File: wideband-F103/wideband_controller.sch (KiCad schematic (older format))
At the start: 107 parts, among them J1 FTSH-107-01-F-DV-K, J2 Conn_02x06_Top_Bottom, J3 Conn_02x02_Odd_Even, J4 Conn_01x10, Q1 VBA2625, Q2 BTS3028, U1 MCP6004, U2 STM32F103C6Tx, U3 OPA388IDR, U4 LM78M05_TO252, U5 XC6206P332MR, U6 REF3033, U7 MCP6002-xSN, U8 TJA1051T-3

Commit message: Addressed issue #19
Added bottom silk for all connector pins.
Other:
- moved on the sheet: C1, C2, C3, C38, C39, C4, C40, C41, C5, C6, J4, R16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

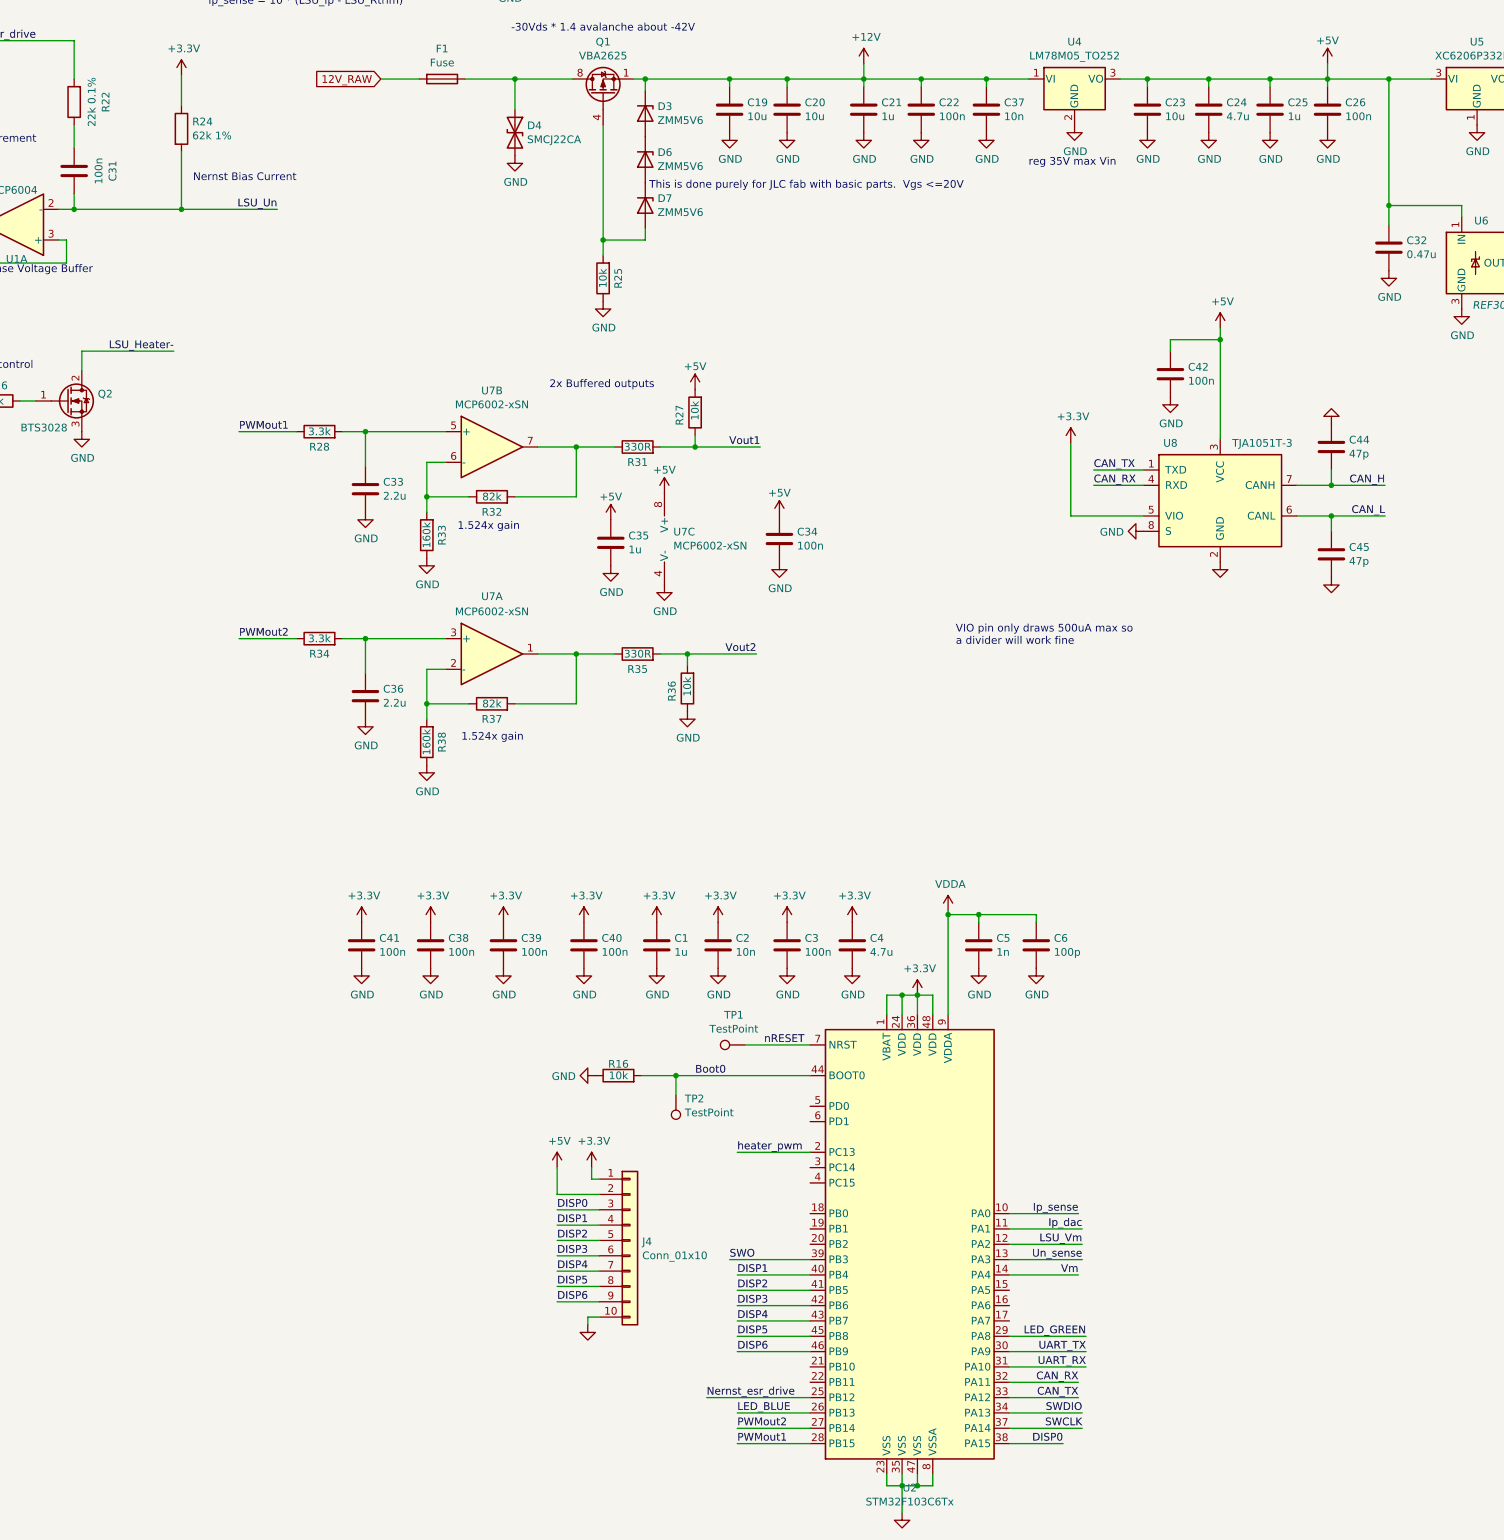
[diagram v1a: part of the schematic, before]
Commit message: 0402 we go!
Changed as many parts as make sense to 0402.  Eliminated several BOM lines.  Added two 0402 solder jumpers for config.  Need to review when less tired.
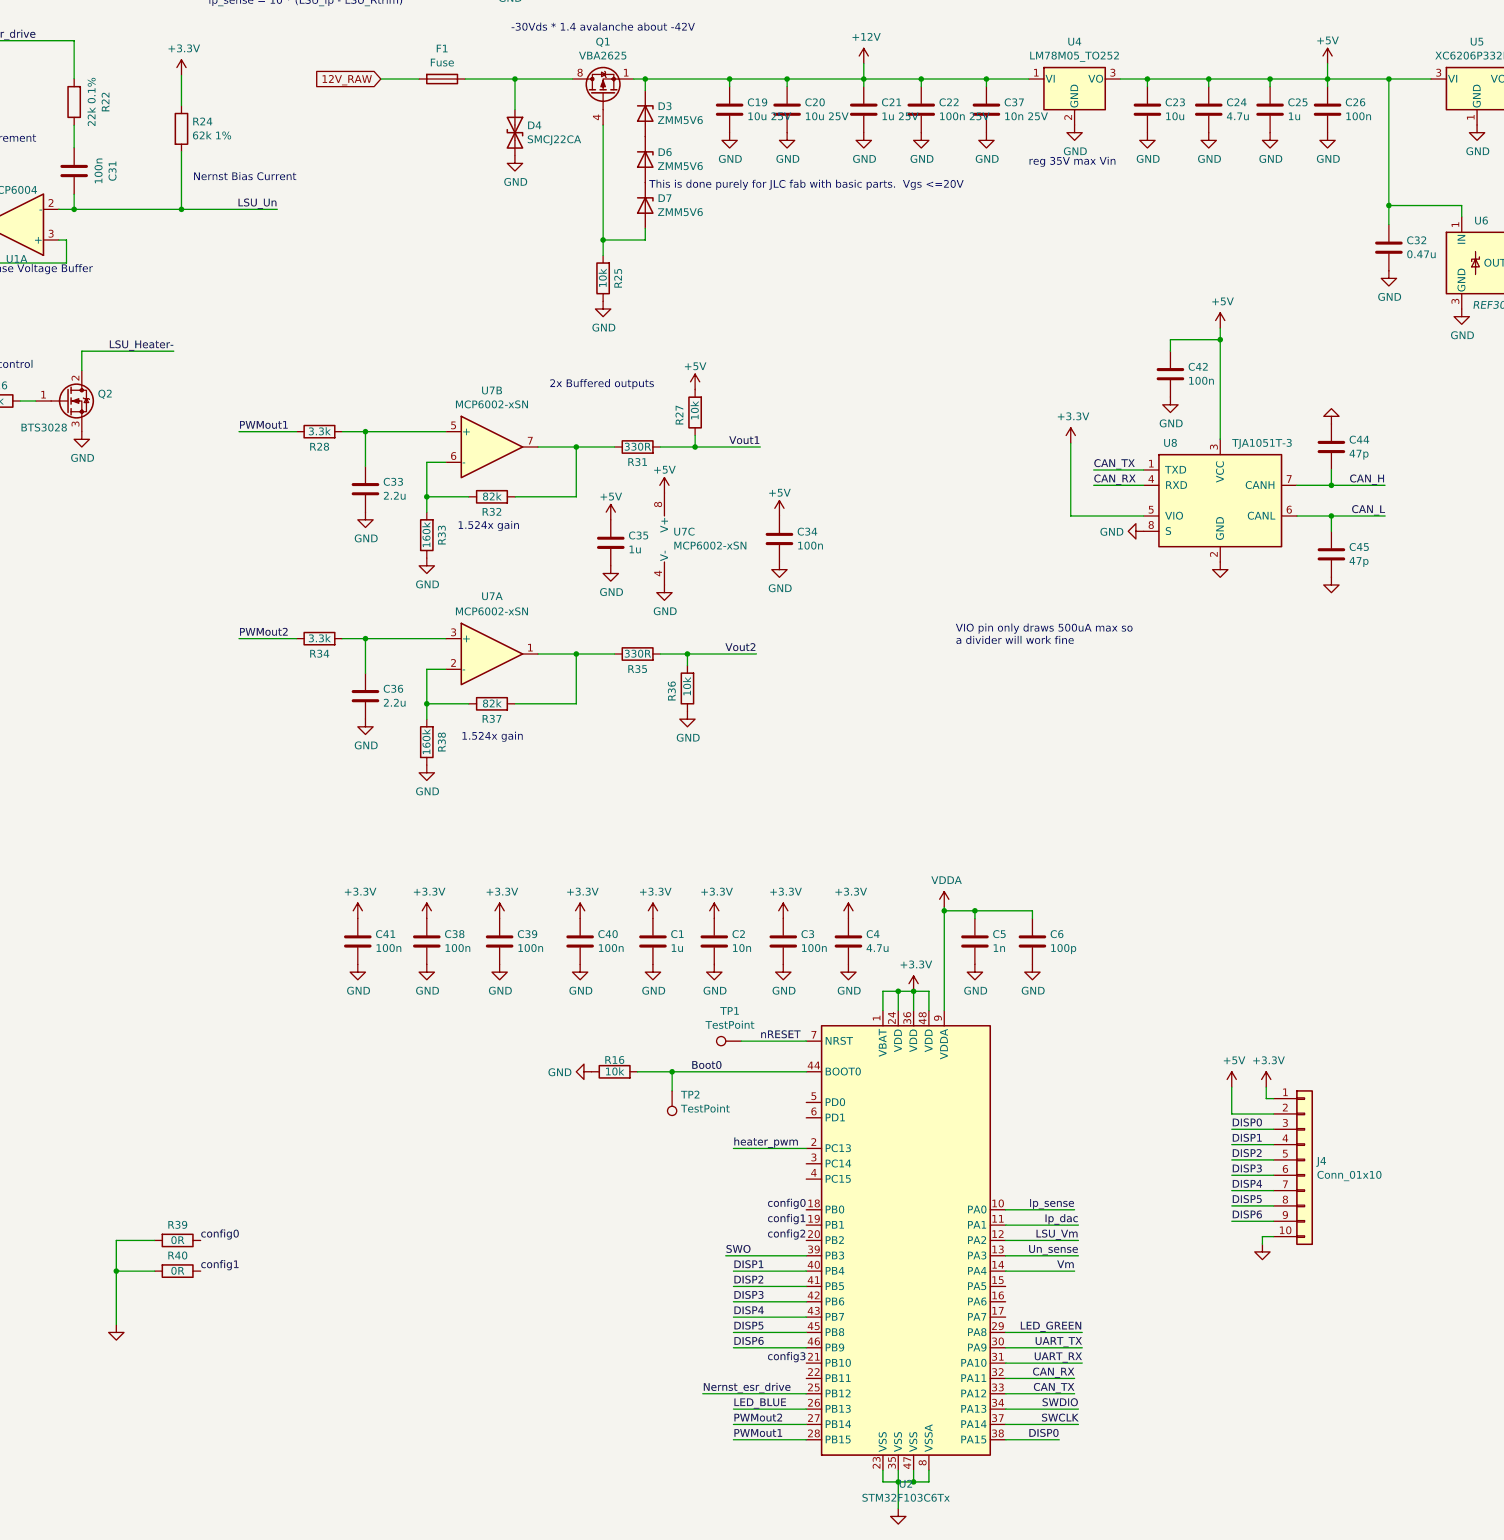
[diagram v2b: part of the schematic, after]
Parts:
- added R39, R40: 0R, Resistor_SMD:R_0402_1005Metric, symbol Device:R
- C1, C10, C25, C28, C35, C7, C8: footprint Capacitor_SMD:C_0603_1608Metric -> Capacitor_SMD:C_0402_1005Metric; LCSC C15849 -> C52923
- C19, C20: value 10u -> 10u 25V
- C21: value 1u -> 1u 25V
- C22: value 100n -> 100n 25V
- C23, C30: footprint Capacitor_SMD:C_0603_1608Metric -> Capacitor_SMD:C_0402_1005Metric; LCSC C19702 -> C15525
- C24, C29, C4: footprint Capacitor_SMD:C_0603_1608Metric -> Capacitor_SMD:C_0402_1005Metric; LCSC C19666 -> C23733
- C32: footprint Capacitor_SMD:C_0603_1608Metric -> Capacitor_SMD:C_0402_1005Metric; LCSC C1623 -> C47339
- C33, C36: footprint Capacitor_SMD:C_0603_1608Metric -> Capacitor_SMD:C_0402_1005Metric; LCSC C23630 -> C12530
- C37: value 10n -> 10n 25V; footprint Capacitor_SMD:C_0603_1608Metric -> Capacitor_SMD:C_0402_1005Metric; LCSC C57112 -> C15195
- R18: footprint Resistor_SMD:R_0603_1608Metric -> Resistor_SMD:R_0402_1005Metric; LCSC C56053 -> 25890
- R28, R34: footprint Resistor_SMD:R_0603_1608Metric -> Resistor_SMD:R_0402_1005Metric; LCSC C22978 -> C25890
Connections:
- net GND: now also R39.2, R40.2
- net config0: now reaches U2.18 (PB0)
- net config0: now also R39.1
- net config1: now reaches U2.19 (PB1)
- net config1: now also R40.1
- net config2: now reaches U2.20 (PB2)
- net config3: now reaches U2.21 (PB10)
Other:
- moved on the sheet: C1, C2, C3, C38, C39, C4, C40, C41, C5, C6, J4, R16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

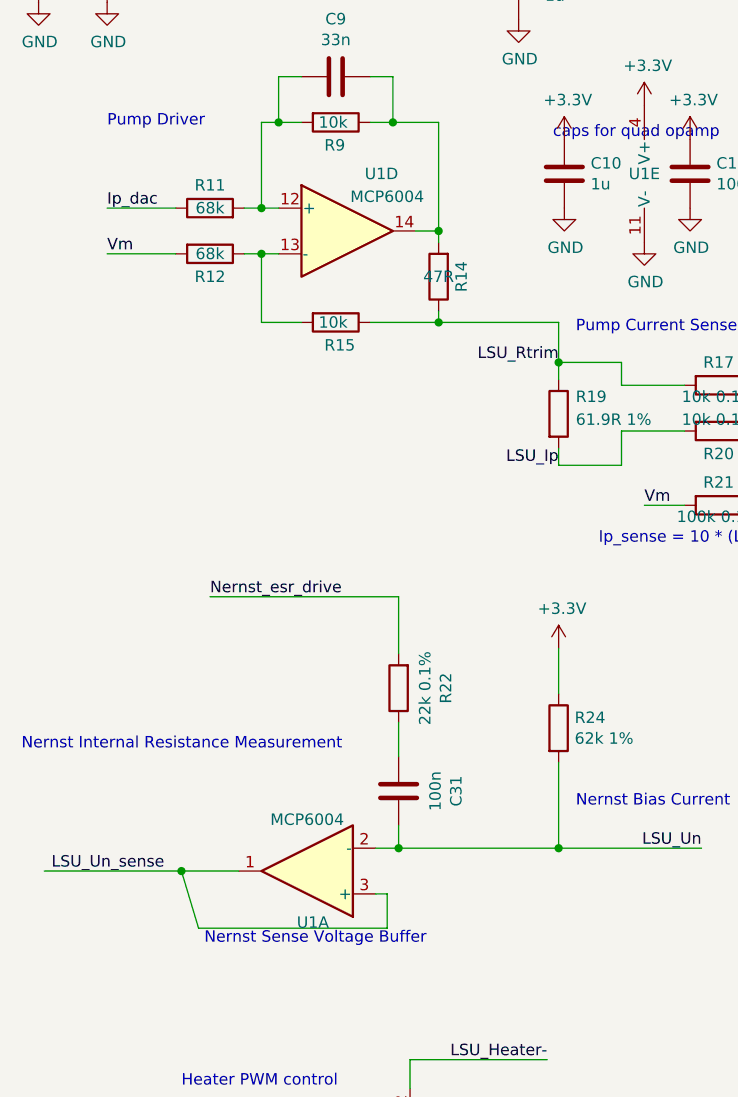
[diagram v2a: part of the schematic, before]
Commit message: Add files via upload
U1A/U1D + and - reversal fixed.  Kept same unobtanium precision op-amp for now.  Incorporates config jumper additions
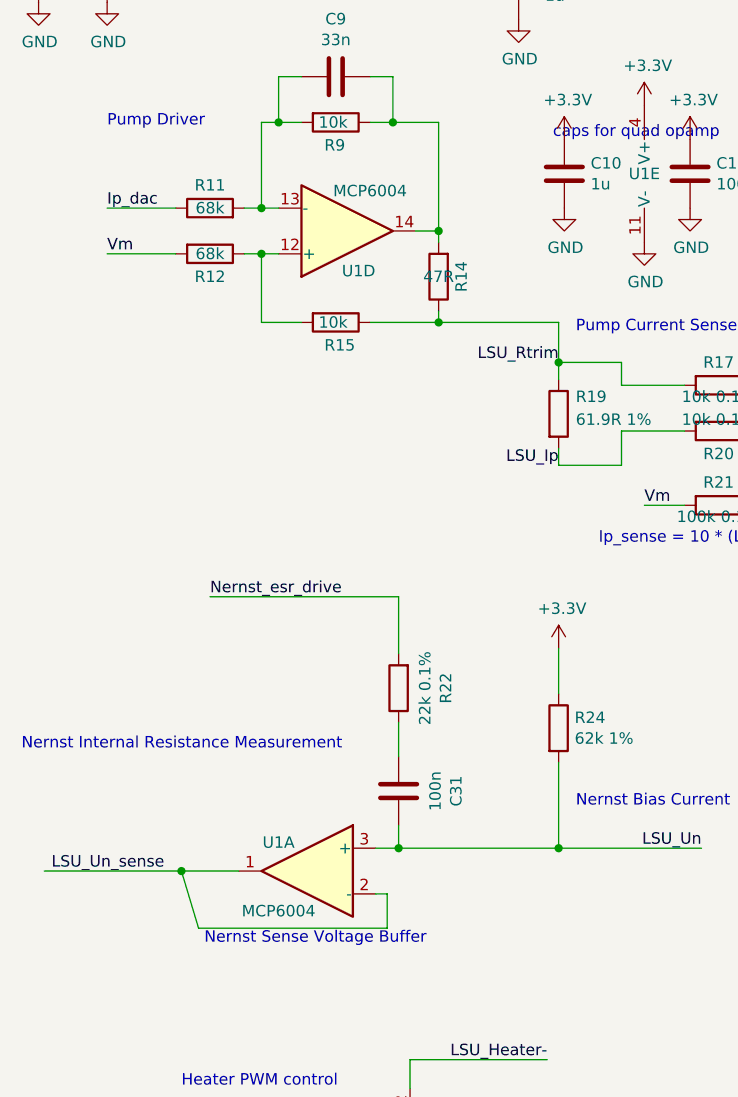
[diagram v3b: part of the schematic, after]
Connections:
- net LSU_Un: now also U1.3 (+); no longer U1.2 (-)
- net LSU_Un_sense: now also U1.2 (-); no longer U1.3 (+)
- net at R12.1, R15.2: now also U1.12 (+); no longer U1.13 (-)
- net at C9.2, R11.2, R9.2: now also U1.13 (-); no longer U1.12 (+)
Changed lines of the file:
@@
 U 1 1 5F8980DF
 P 1975 5475
-F 0 "U1" H 1950 5700 50  0000 C CNN
-F 1 "MCP6004" H 1975 5250 50  0000 C CNN
+F 0 "U1" H 2100 5600 50  0000 C CNN
+F 1 "MCP6004" H 2100 5300 50  0000 C CNN
 F 2 "Package_SO:TSSOP-14_4.4x5mm_P0.65mm" H 1925 5575 50  0001 C CNN
 F 3 "http://ww1.microchip.com/downloads/en/DeviceDoc/21733j.pdf" H 2025 5675 50  0001 C CNN
 F 4 "C50282" H 1975 5475 50  0001 C CNN "LCSC"
 	1    1975 5475
-	-1   0    0    1
+	-1   0    0    -1
 $EndComp
 Wire Wire Line
@@
 U 4 1 5F8B9D88
 P 2150 2675
-F 0 "U1" H 2300 2925 50  0000 C CNN
-F 1 "MCP6004" H 2325 2825 50  0000 C CNN
+F 0 "U1" H 2200 2850 50  0000 C CNN
+F 1 "MCP6004" H 2250 2500 50  0000 C CNN
 F 2 "Package_SO:TSSOP-14_4.4x5mm_P0.65mm" H 2100 2775 50  0001 C CNN
 F 3 "http://ww1.microchip.com/downloads/en/DeviceDoc/21733j.pdf" H 2200 2875 50  0001 C CNN
 F 4 "C50282" H 2150 2675 50  0001 C CNN "LCSC"
 	4    2150 2675
-	1    0    0    -1
-$EndComp
-$Comp
+	1    0    0    1
+$EndComp
+$Comp

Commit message: Switched precision opamp
Switched to SOT23-5 precision op-amp.  Specifying GS8331 chopper (good stock as of commit) but should work with AD8628 as originally specified.
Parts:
- removed U3: OPA388IDR, Package_SO:SOIC-8_3.9x4.9mm_P1.27mm, symbol Amplifier_Operational:OPA376xxD
- added U3: GS8331, Package_TO_SOT_SMD:SOT-23-5, symbol Amplifier_Operational:OPA842xDBV
- R18: value 3.3k 1% -> 3.3k 0.1%; footprint Resistor_SMD:R_0402_1005Metric -> Resistor_SMD:R_0805_2012Metric; LCSC 25890 -> C186265
- TP1, TP2: footprint Connector_PinHeader_2.54mm:PinHeader_1x01_P2.54mm_Horizontal -> Connector_PinHeader_2.54mm:PinHeader_1x01_P2.54mm_Vertical
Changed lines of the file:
@@
 P 5000 3450
 F 0 "R18" V 4793 3450 50  0000 C CNN
-F 1 "3.3k 1%" V 4884 3450 50  0000 C CNN
-F 2 "Resistor_SMD:R_0402_1005Metric" V 4930 3450 50  0001 C CNN
+F 1 "3.3k 0.1%" V 4884 3450 50  0000 C CNN
+F 2 "Resistor_SMD:R_0805_2012Metric" V 4930 3450 50  0001 C CNN
 F 3 "~" H 5000 3450 50  0001 C CNN
-F 4 "25890" H 5000 3450 50  0001 C CNN "LCSC"
+F 4 "C186265" H 5000 3450 50  0001 C CNN "LCSC"
 	1    5000 3450
 	0    -1   1    0
@@
 	8925 12100 8450 12100
 $Comp
-L Amplifier_Operational:OPA376xxD U3
-U 1 1 5FD9F83A
-P 4350 3450
-F 0 "U3" H 4375 3300 50  0000 L CNN
-F 1 "OPA388IDR" H 4375 3625 50  0000 L CNN
-F 2 "Package_SO:SOIC-8_3.9x4.9mm_P1.27mm" H 4250 3250 50  0001 L CNN
-F 3 "https://datasheet.lcsc.com/szlcsc/Texas-Instruments-TI-OPA388IDR_C154118.pdf" H 4500 3600 50  0001 C CNN
-F 4 "C154118" H 4350 3450 50  0001 C CNN "LCSC"
-	1    4350 3450
-	1    0    0    1
-$EndComp
-$Comp
 L Device:R R19
 U 1 1 5FEE6D7F
@@
 F 0 "TP1" V 6920 10872 50  0000 C CNN
 F 1 "TestPoint" V 6829 10872 50  0000 C CNN
-F 2 "Connector_PinHeader_2.54mm:PinHeader_1x01_P2.54mm_Horizontal" H 6925 10800 50  0001 C CNN
+F 2 "Connector_PinHeader_2.54mm:PinHeader_1x01_P2.54mm_Vertical" H 6925 10800 50  0001 C CNN
 F 3 "~" H 6925 10800 50  0001 C CNN
 	1    6725 10800
@@
 F 0 "TP2" H 6217 11151 50  0000 R CNN
 F 1 "TestPoint" H 6217 11242 50  0000 R CNN
-F 2 "Connector_PinHeader_2.54mm:PinHeader_1x01_P2.54mm_Horizontal" H 6475 11125 50  0001 C CNN
+F 2 "Connector_PinHeader_2.54mm:PinHeader_1x01_P2.54mm_Vertical" H 6475 11125 50  0001 C CNN
 F 3 "~" H 6475 11125 50  0001 C CNN
 	1    6275 11125
@@
 Wire Wire Line
 	2650 12300 2650 12650
+$Comp
+L Amplifier_Operational:OPA842xDBV U3
+U 1 1 61F513E4
+P 4350 3450
+F 0 "U3" H 4350 2969 50  0000 C CNN
+F 1 "GS8331" H 4350 3060 50  0000 C CNN
+F 2 "Package_TO_SOT_SMD:SOT-23-5" H 4250 3250 50  0001 L CNN
+F 3 "https://datasheet.lcsc.com/lcsc/1810211711_Gainsil-GS8331-TR_C157712.pdf" H 4350 3650 50  0001 C CNN
+F 4 "C157712" H 4350 3450 50  0001 C CNN "LCSC"
+	1    4350 3450
+	1    0    0    1
+$EndComp
 $EndSCHEMATC
